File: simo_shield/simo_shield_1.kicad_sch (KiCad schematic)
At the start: 11 parts, among them J1 Conn_01x02_Female, J2 Conn_01x02_Female, J3 Conn_01x01_Female, U1 elemon_board, U2 modulo_flash_externa, U3 bluepill_board_stm32, U4 modulo_acelerometro

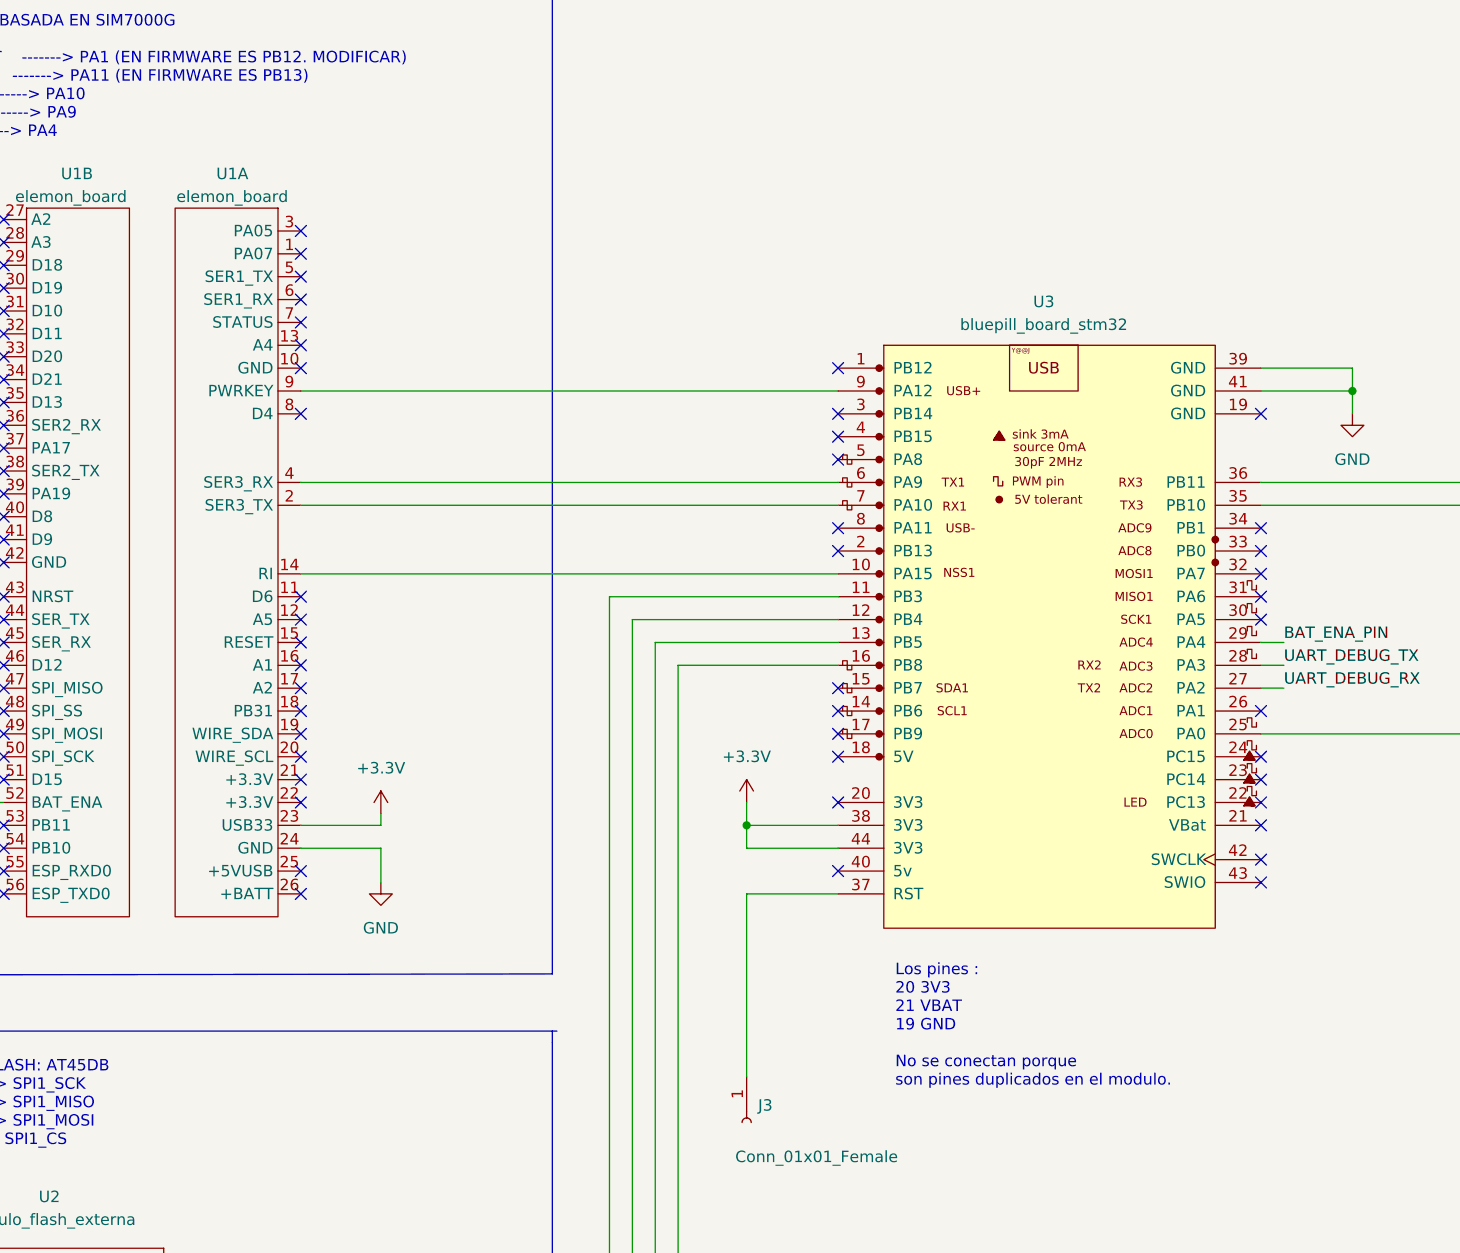
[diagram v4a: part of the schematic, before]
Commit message: se hizo mas compacto el PCB
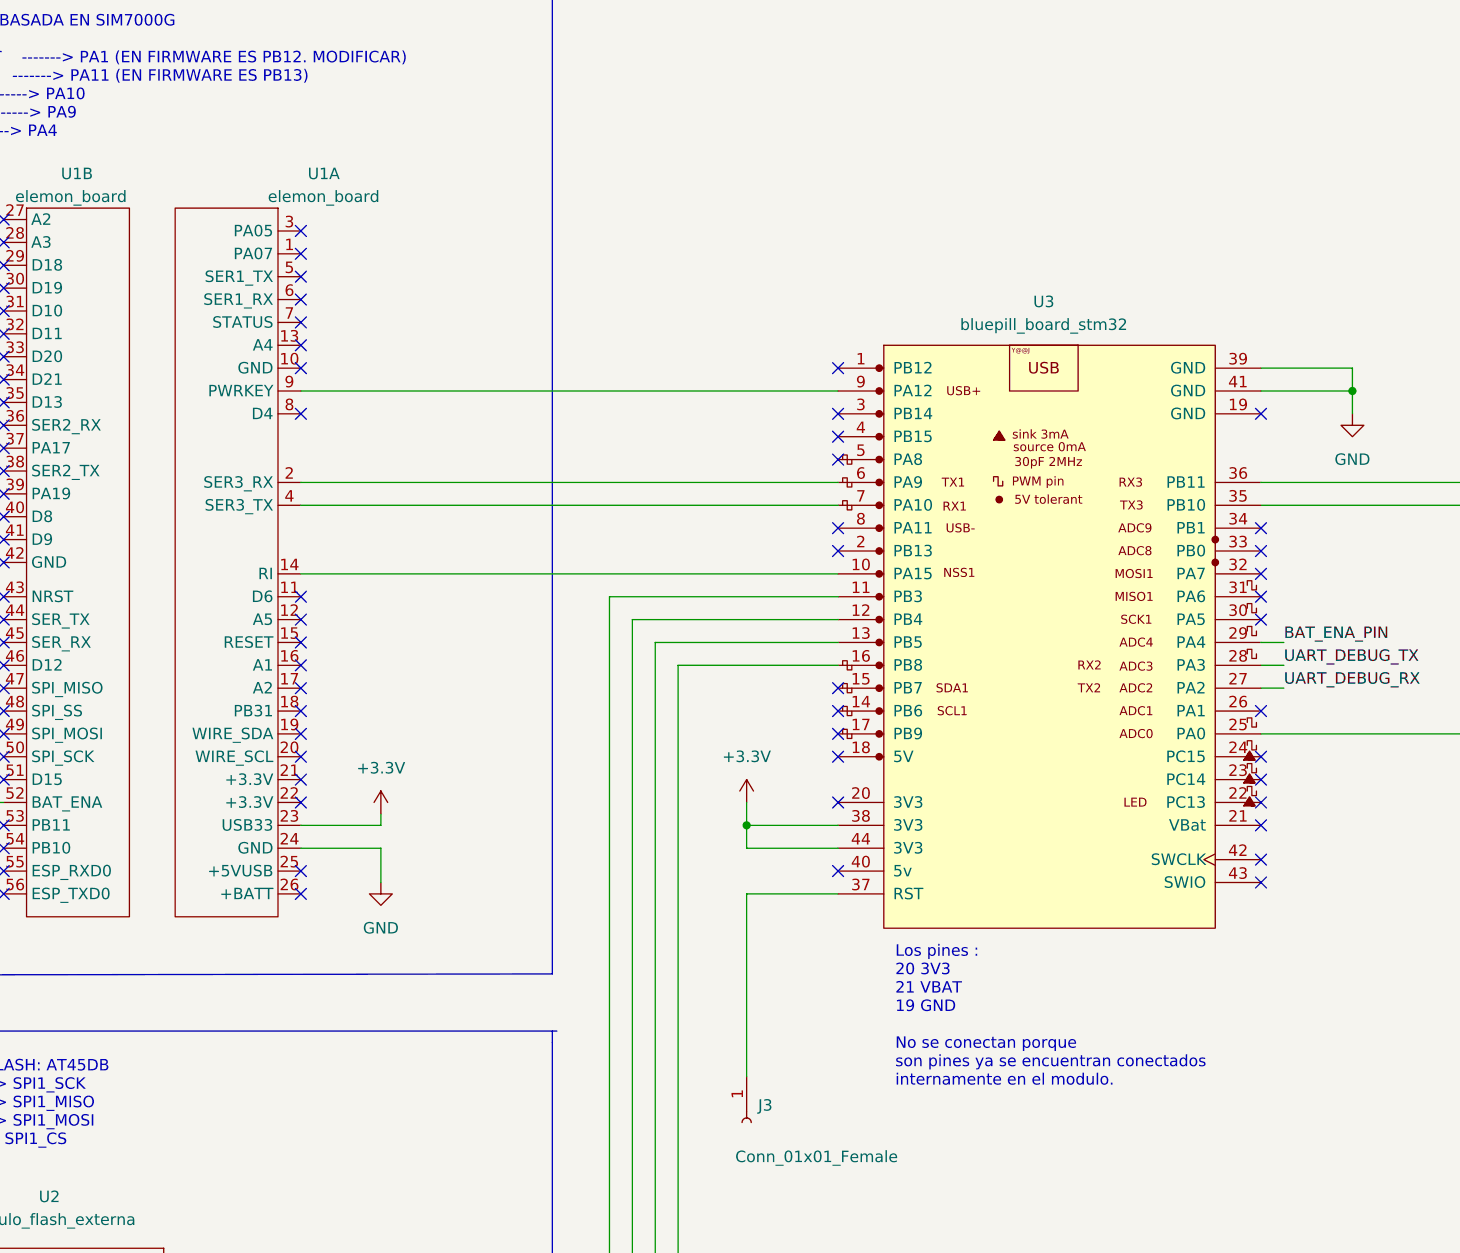
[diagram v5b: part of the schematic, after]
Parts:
- U1: footprint simo_shield:elemon_board -> simo_shield:elemon_board_compacto
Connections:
- net at U1.2 (SER3_RX): now also U3.6 (PA9); no longer U3.7 (PA10)
- net at U1.4 (SER3_TX): now also U3.7 (PA10); no longer U3.6 (PA9)
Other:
- note added: "Los pines : 20 3V3 21 VBAT 19 GND No se conectan porque son pines ya se encuentran conectados internamente en el modulo."
- note removed: "Los pines : 20 3V3 21 VBAT 19 GND No se conectan porque son pines duplicados en el modulo."
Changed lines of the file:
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@@
+    (stroke (width 0) (type default) (color 0 0 0 0))
+  )
+  (wire (pts (xy 76.2 109.22) (xy 76.2 110.49))
+    (stroke (width 0) (type default) (color 0 0 0 0))
+  )
+  (polyline (pts (xy 199.263 122.047) (xy 199.263 118.999))
+    (stroke (width 0) (type default) (color 0 0 0 0))
+  )
+  (polyline (pts (xy 95.25 133.35) (xy 95.25 134.62))
+    (stroke (width 0) (type default) (color 0 0 0 0))
+  )
+  (polyline (pts (xy 199.263 141.097) (xy 199.263 121.539))
+    (stroke (width 0) (type default) (color 0 0 0 0))
+  )
+  (polyline (pts (xy 13.843 127.127) (xy 13.843 15.875))
+    (stroke (width 0) (type default) (color 0 0 0 0))
+  )
+  (polyline (pts (xy 13.589 188.214) (xy 13.97 134.112))
+    (stroke (width 0) (type default) (color 0 0 0 0))
+  )
+  (wire (pts (xy 224.155 129.54) (xy 236.22 129.54))
+    (stroke (width 0) (type default) (color 0 0 0 0))
+  )
+  (wire (pts (xy 30.48 107.95) (xy 34.29 107.95))
+    (stroke (width 0) (type default) (color 0 0 0 0))
+  )
+  (wire (pts (xy 54.61 172.72) (xy 109.22 172.72))
+    (stroke (width 0) (type default) (color 0 0 0 0))
+  )
+  (polyline (pts (xy 199.644 118.999) (xy 282.956 118.872))
+    (stroke (width 0) (type default) (color 0 0 0 0))
+  )
+  (wire (pts (xy 106.68 90.17) (xy 106.68 170.18))
+    (stroke (width 0) (type default) (color 0 0 0 0))
+  )
+  (polyline (pts (xy 283.21 87.63) (xy 283.21 113.03))
+    (stroke (width 0) (type default) (color 0 0 0 0))
+  )
+  (wire (pts (xy 109.22 92.71) (xy 127 92.71))
+    (stroke (width 0) (type default) (color 0 0 0 0))
+  )
+  (polyline (pts (xy 199.263 118.999) (xy 199.644 118.999))
+    (stroke (width 0) (type default) (color 0 0 0 0))
+  )
+  (polyline (pts (xy 17.78 15.875) (xy 95.25 15.748))
+    (stroke (width 0) (type default) (color 0 0 0 0))
+  )
+  (polyline (pts (xy 283.21 140.97) (xy 199.263 141.097))
+    (stroke (width 0) (type default) (color 0 0 0 0))
+  )
+  (wire (pts (xy 67.31 62.23) (xy 127 62.23))
+    (stroke (width 0) (type default) (color 0 0 0 0))
+  )
+  (wire (pts (xy 212.09 77.47) (xy 223.52 77.47))
+    (stroke (width 0) (type default) (color 0 0 0 0))
+  )
+  (polyline (pts (xy 283.21 113.03) (xy 199.39 113.03))
+    (stroke (width 0) (type default) (color 0 0 0 0))
+  )
+  (wire (pts (xy 212.09 80.01) (xy 223.52 80.01))
+    (stroke (width 0) (type default) (color 0 0 0 0))
+  )
+  (polyline (pts (xy 95.25 134.62) (xy 95.25 187.071))
+    (stroke (width 0) (type default) (color 0 0 0 0))
+  )
+  (wire (pts (xy 101.6 85.09) (xy 127 85.09))
+    (stroke (width 0) (type default) (color 0 0 0 0))
+  )
+  (polyline (pts (xy 13.843 15.875) (xy 17.78 15.875))
+    (stroke (width 0) (type default) (color 0 0 0 0))
+  )
+  (wire (pts (xy 104.14 167.64) (xy 104.14 87.63))
+    (stroke (width 0) (type default) (color 0 0 0 0))
+  )
+  (wire (pts (xy 67.31 113.03) (xy 76.2 113.03))
+    (stroke (width 0) (type default) (color 0 0 0 0))
+  )
+  (wire (pts (xy 173.99 62.23) (xy 184.15 62.23))
+    (stroke (width 0) (type default) (color 0 0 0 0))
+  )
+  (polyline (pts (xy 283.21 40.64) (xy 283.21 83.82))
+    (stroke (width 0) (type default) (color 0 0 0 0))
+  )
+  (wire (pts (xy 76.2 113.03) (xy 76.2 116.84))
+    (stroke (width 0) (type default) (color 0 0 0 0))
+  )
+  (polyline (pts (xy 199.39 87.63) (xy 283.21 87.63))
+    (stroke (width 0) (type default) (color 0 0 0 0))
+  )
+  (wire (pts (xy 173.99 100.33) (xy 223.52 100.33))
     (stroke (width 0) (type default) (color 0 0 0 0))
   )
@@
     (stroke (width 0) (type default) (color 0 0 0 0))
   )
-  (wire (pts (xy 76.2 109.22) (xy 76.2 110.49))
-    (stroke (width 0) (type default) (color 0 0 0 0))
-  )
-  (polyline (pts (xy 199.263 122.047) (xy 199.263 118.999))
-    (stroke (width 0) (type default) (color 0 0 0 0))
-  )
-  (polyline (pts (xy 95.25 133.35) (xy 95.25 134.62))
-    (stroke (width 0) (type default) (color 0 0 0 0))
-  )
-  (polyline (pts (xy 199.263 141.097) (xy 199.263 121.539))
-    (stroke (width 0) (type default) (color 0 0 0 0))
-  )
-  (polyline (pts (xy 13.843 127.127) (xy 13.843 15.875))
-    (stroke (width 0) (type default) (color 0 0 0 0))
-  )
-  (polyline (pts (xy 13.589 188.214) (xy 13.97 134.112))
-    (stroke (width 0) (type default) (color 0 0 0 0))
-  )
-  (wire (pts (xy 224.155 129.54) (xy 236.22 129.54))
-    (stroke (width 0) (type default) (color 0 0 0 0))
-  )
-  (wire (pts (xy 30.48 107.95) (xy 34.29 107.95))
-    (stroke (width 0) (type default) (color 0 0 0 0))
-  )
-  (wire (pts (xy 54.61 172.72) (xy 109.22 172.72))
-    (stroke (width 0) (type default) (color 0 0 0 0))
-  )
-  (polyline (pts (xy 199.644 118.999) (xy 282.956 118.872))
-    (stroke (width 0) (type default) (color 0 0 0 0))
-  )
-  (wire (pts (xy 106.68 90.17) (xy 106.68 170.18))
-    (stroke (width 0) (type default) (color 0 0 0 0))
-  )
-  (polyline (pts (xy 283.21 87.63) (xy 283.21 113.03))
-    (stroke (width 0) (type default) (color 0 0 0 0))
-  )
-  (wire (pts (xy 109.22 92.71) (xy 127 92.71))
-    (stroke (width 0) (type default) (color 0 0 0 0))
-  )
-  (polyline (pts (xy 199.263 118.999) (xy 199.644 118.999))
-    (stroke (width 0) (type default) (color 0 0 0 0))
-  )
-  (polyline (pts (xy 17.78 15.875) (xy 95.25 15.748))
-    (stroke (width 0) (type default) (color 0 0 0 0))
-  )
-  (polyline (pts (xy 283.21 140.97) (xy 199.263 141.097))
-    (stroke (width 0) (type default) (color 0 0 0 0))
-  )
-  (wire (pts (xy 67.31 62.23) (xy 127 62.23))
-    (stroke (width 0) (type default) (color 0 0 0 0))
-  )
-  (wire (pts (xy 212.09 77.47) (xy 223.52 77.47))
-    (stroke (width 0) (type default) (color 0 0 0 0))
-  )
-  (polyline (pts (xy 283.21 113.03) (xy 199.39 113.03))
-    (stroke (width 0) (type default) (color 0 0 0 0))
-  )
-  (wire (pts (xy 212.09 80.01) (xy 223.52 80.01))
-    (stroke (width 0) (type default) (color 0 0 0 0))
-  )
-  (polyline (pts (xy 95.25 134.62) (xy 95.25 187.071))
-    (stroke (width 0) (type default) (color 0 0 0 0))
-  )
-  (wire (pts (xy 101.6 85.09) (xy 127 85.09))
-    (stroke (width 0) (type default) (color 0 0 0 0))
-  )
-  (polyline (pts (xy 13.843 15.875) (xy 17.78 15.875))
-    (stroke (width 0) (type default) (color 0 0 0 0))
-  )
-  (wire (pts (xy 104.14 167.64) (xy 104.14 87.63))
-    (stroke (width 0) (type default) (color 0 0 0 0))
-  )
-  (wire (pts (xy 67.31 113.03) (xy 76.2 113.03))
-    (stroke (width 0) (type default) (color 0 0 0 0))
-  )
-  (wire (pts (xy 173.99 62.23) (xy 184.15 62.23))
-    (stroke (width 0) (type default) (color 0 0 0 0))
-  )
-  (polyline (pts (xy 283.21 40.64) (xy 283.21 83.82))
-    (stroke (width 0) (type default) (color 0 0 0 0))
-  )
-  (wire (pts (xy 76.2 113.03) (xy 76.2 116.84))
-    (stroke (width 0) (type default) (color 0 0 0 0))
-  )
-  (polyline (pts (xy 199.39 87.63) (xy 283.21 87.63))
-    (stroke (width 0) (type default) (color 0 0 0 0))
-  )
-  (wire (pts (xy 173.99 100.33) (xy 223.52 100.33))
-    (stroke (width 0) (type default) (color 0 0 0 0))
-  )
   (polyline (pts (xy 95.25 127) (xy 13.843 127.127))
     (stroke (width 0) (type default) (color 0 0 0 0))
@@
     (effects (font (size 1.27 1.27)) (justify left bottom))
   )
-  (text "Los pines :\n20 3V3\n21 VBAT\n19 GND\n\nNo se conectan porque \nson pines duplicados en el modulo."
+  (text "Los pines :\n20 3V3\n21 VBAT\n19 GND\n\nNo se conectan porque \nson pines ya se encuentran conectados \ninternamente en el modulo."
     (at 133.35 139.7 0)
     (effects (font (size 1.27 1.27)) (justify left bottom))
@@
     (pin "1")
   )
-  (symbol (lib_id "simo_shield:elemon_board") (at 64.77 40.64 0) (mirror y) (unit 1)
+  (symbol (lib_name "elemon_board_1") (lib_id "simo_shield:elemon_board") (at 64.77 40.64 0) (mirror y) (unit 1)
     (in_bom yes) (on_board yes)
-    (property "Reference" "U1" (id 0) (at 59.69 38.1 0))
-    (property "Value" "elemon_board" (id 1) (at 59.69 40.64 0))
-    (property "Footprint" "simo_shield:elemon_board" (id 2) (at 90.17 41.91 0)
+    (property "Reference" "U1" (id 0) (at 69.85 38.1 0))
+    (property "Value" "elemon_board" (id 1) (at 69.85 40.64 0))
+    (property "Footprint" "simo_shield:elemon_board_compacto" (id 2) (at 39.37 41.91 0)
       (effects (font (size 1.27 1.27)) hide)
     )
@@
       (effects (font (size 1.27 1.27)) (justify left))
     )
-    (property "Footprint" "simo_shield:elemon_board" (id 2) (at 11.43 41.91 0)
+    (property "Footprint" "simo_shield:elemon_board_compacto" (id 2) (at 11.43 41.91 0)
       (effects (font (size 1.27 1.27)) hide)
     )
@@
     )
     (path "/5da0ae67-8451-47ba-8f38-5b0fec97941b"
-      (reference "U1") (unit 1) (value "elemon_board") (footprint "simo_shield:elemon_board")
+      (reference "U1") (unit 1) (value "elemon_board") (footprint "simo_shield:elemon_board_compacto")
     )
     (path "/c6805e71-a6e7-4702-ae04-729e6ae6705d"
-      (reference "U1") (unit 2) (value "elemon_board") (footprint "simo_shield:elemon_board")
+      (reference "U1") (unit 2) (value "elemon_board") (footprint "simo_shield:elemon_board_compacto")
     )
     (path "/50ab3c25-18ac-4348-9b10-e46fc412d281"
